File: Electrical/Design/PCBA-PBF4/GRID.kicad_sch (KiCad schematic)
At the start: 9 parts, among them J703 AFB10-S08LCA-00, J704 AFB10-S08LCA-00, J705 AFB10-S08LCA-00, J706 AFB10-S08LCA-00, J707 AFB10-S08LCA-00, J708 AFB10-S08LCA-00, J709 AFB10-S08LCA-00, J710 AFB10-S08LCA-00, M701 (NF)

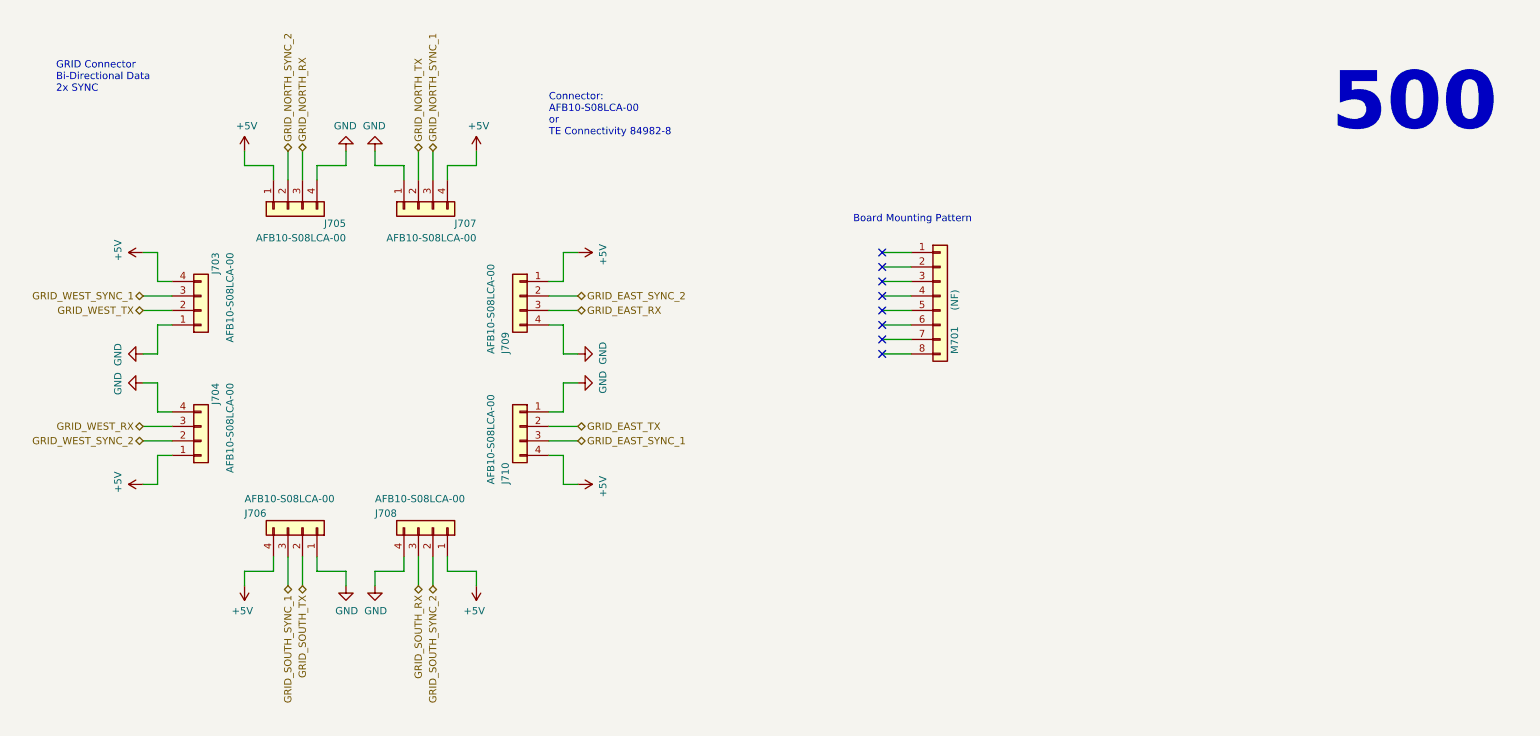
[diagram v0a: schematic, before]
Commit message: SUKU pcbs updated with footprint and symbol values
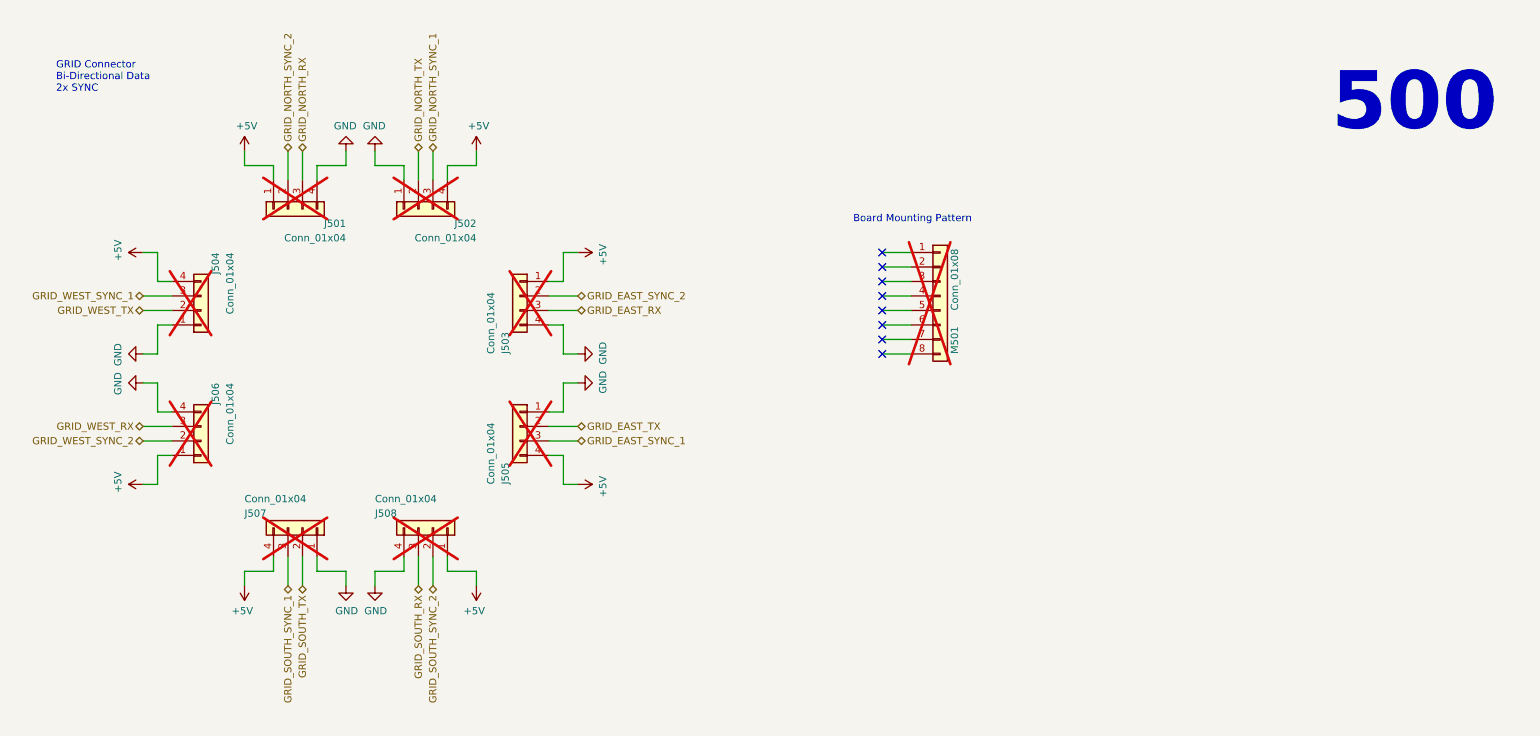
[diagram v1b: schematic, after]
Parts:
- J501: renamed from J705; value AFB10-S08LCA-00 -> Conn_01x04; now not fitted
- J502: renamed from J707; value AFB10-S08LCA-00 -> Conn_01x04; now not fitted
- J503: renamed from J709; value AFB10-S08LCA-00 -> Conn_01x04; now not fitted
- J504: renamed from J703; value AFB10-S08LCA-00 -> Conn_01x04; now not fitted
- J505: renamed from J710; value AFB10-S08LCA-00 -> Conn_01x04; now not fitted
- J506: renamed from J704; value AFB10-S08LCA-00 -> Conn_01x04; now not fitted
- J507: renamed from J706; value AFB10-S08LCA-00 -> Conn_01x04; now not fitted
- J508: renamed from J708; value AFB10-S08LCA-00 -> Conn_01x04; now not fitted
- M501: renamed from M701; value (NF) -> Conn_01x08; now not fitted; now left out of the parts list
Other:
- note removed: "Connector: AFB10-S08LCA-00 or TE Connectivity 84982-8"
